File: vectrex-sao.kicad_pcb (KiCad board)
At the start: 2 copper layers, 78 parts, among them J2 Badgelife_sao_connector_v169b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, U1 PIC16F886-IP, U2 IS31FL3731-SALS2

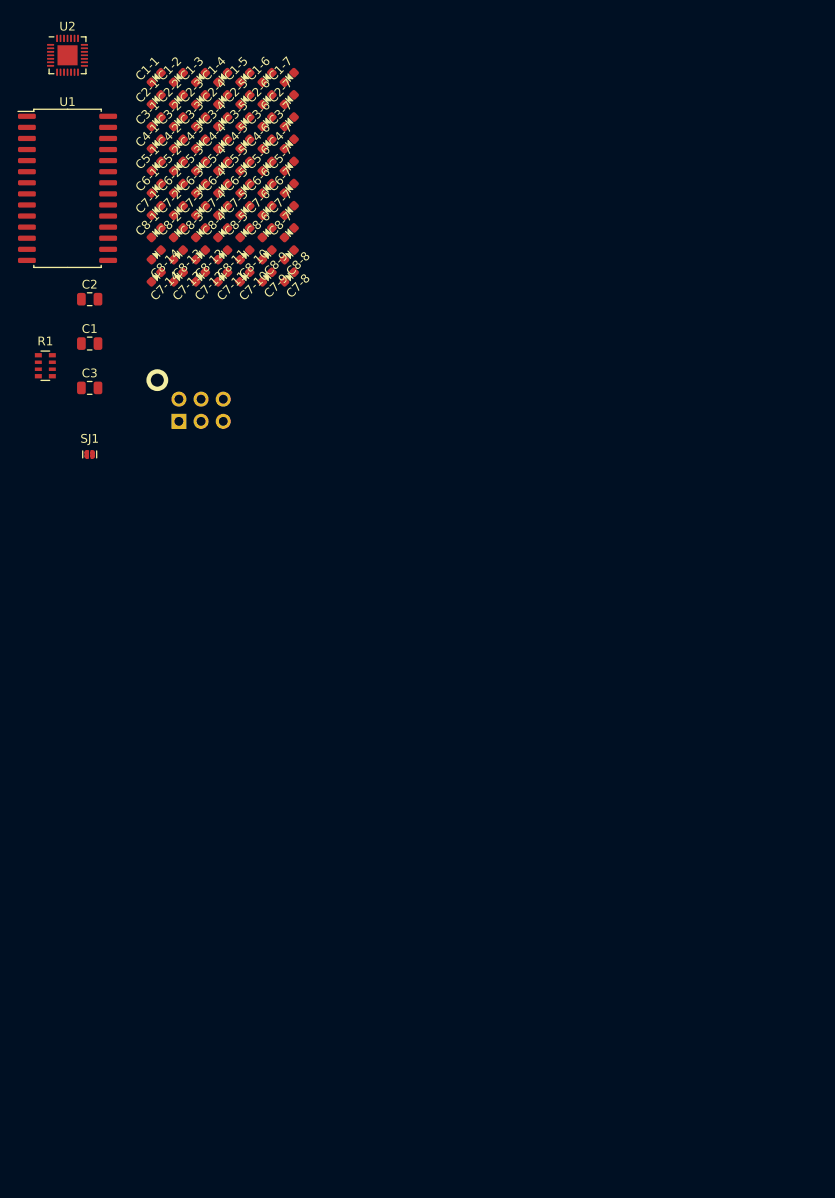
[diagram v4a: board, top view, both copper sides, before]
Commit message: rearranged parts, add temp silk, grid 2.54mm
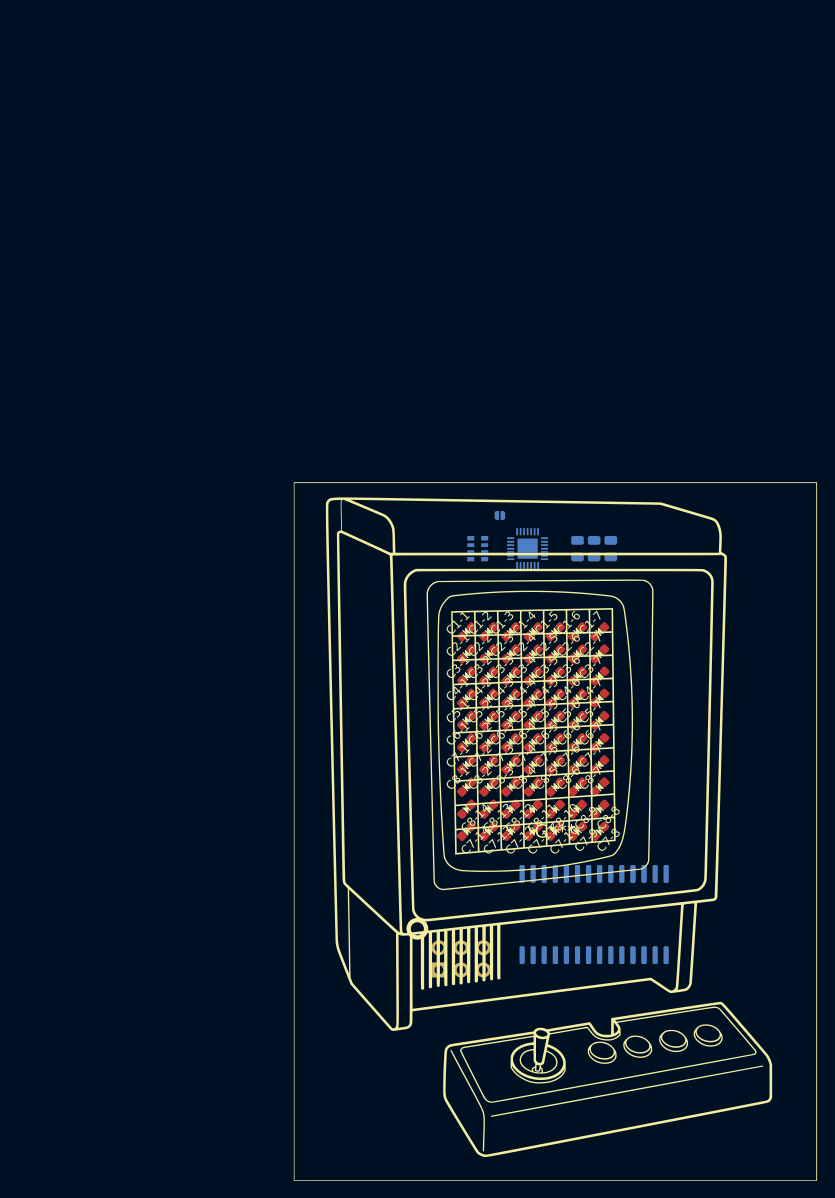
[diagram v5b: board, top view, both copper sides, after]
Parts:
- added G***: LOGO, LOGO, F.Cu at (127.0, 106.7)
- C1, C2, C3, R1, SJ1, U1, U2: moved to B.Cu
- moved U1 102.8 mm to (131.4, 116.2), turned to -90 degrees
- moved U2 77.3 mm to (123.8, 74.3), turned to 180 degrees
- moved C3-7 72.8 mm to (132.1, 88.9)
- moved C7-8 72.8 mm to (132.1, 106.7)
- moved C2-1 72.8 mm to (116.8, 86.4)
- moved C2-2 72.8 mm to (119.4, 86.4)
- moved C2-3 72.8 mm to (121.9, 86.4)
- moved C2-5 72.8 mm to (127.0, 86.4)
- moved C2-7 72.8 mm to (132.1, 86.4)
- moved C3-1 72.8 mm to (116.8, 88.9)
- moved C3-2 72.8 mm to (119.4, 88.9)
- moved C3-3 72.8 mm to (121.9, 88.9)
- moved C3-4 72.8 mm to (124.5, 88.9)
- moved C3-5 72.8 mm to (127.0, 88.9)
- moved C3-6 72.8 mm to (129.5, 88.9)
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
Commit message: finished outline, added controller board
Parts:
- removed the G*** at (127.0, 106.7)
- removed SJ1: SOLDERJUMPER, vectrex-sao:SolderJumper-2_P1.3mm_Open_RoundedPad1.0x1.5mm
- added C4: 0.1uF, Capacitor_SMD:C_0805_2012Metric, B.Cu at (115.0, 71.6)
- added C5: 0.1uF, Capacitor_SMD:C_0603_1608Metric, B.Cu at (124.0, 121.5)
- added C6: 22pF, Capacitor_SMD:C_0603_1608Metric, B.Cu at (126.2, 121.5)
- added G***: vectrex-graphic-console-80mm, vectrex-sao:vectrex-graphic-console-80mm, F.Cu at (125.9, 105.5)
- added J1: ICSP, Connector_PinHeader_2.54mm:PinHeader_1x06_P2.54mm_Vertical_SMD_Pin1Right, B.Cu at (106.1, 98.5)
- added JP1: TOUCH_PAD, vectrex-sao:MountingHole_1.5mm_M2_Pad_TopOnly, B.Cu at (133.8, 117.9)
- added JP3: ADDR, vectrex-sao:SolderJumper-2_P1.3mm_Open_RoundedPad1.0x1.5mm, B.Cu at (118.5, 71.0)
- added JP4: TX, vectrex-sao:SolderJumper-2_P1.3mm_Open_RoundedPad1.0x1.5mm, B.Cu at (106.0, 114.5)
- added JP5: RX, vectrex-sao:SolderJumper-2_P1.3mm_Open_RoundedPad1.0x1.5mm, B.Cu at (104.2, 114.5)
- added R2: 10k, Resistor_SMD:R_0603_1608Metric, B.Cu at (125.5, 115.5)
- added R3: 1k, Resistor_SMD:R_0603_1608Metric, B.Cu at (128.7, 120.8)
- added U3: TC233A, Package_TO_SOT_SMD:SOT-23-6, B.Cu at (125.1, 118.2)
- C1-1, C1-2, C1-3, C1-4, C1-5, C1-6, C1-7, C2-1, C2-2, C2-3, C2-4, C2-5, C2-6, C2-7, C3-1, C3-2, C3-3, C3-4, C3-5, C3-6, C3-7, C4-1, C4-2, C4-3, C4-4, C4-5, C4-6, C4-7, C5-1, C5-2, C5-3, C5-4, C5-5, C5-6, C5-7, C6-1, C6-2, C6-3, C6-4, C6-5, C6-6, C6-7, C7-1, C7-10, C7-11, C7-12, C7-13, C7-14, C7-2, C7-3, C7-4, C7-5, C7-6, C7-7, C7-8, C7-9, C8-1, C8-10, C8-11, C8-12, C8-13, C8-14, C8-2, C8-3, C8-4, C8-5, C8-6, C8-7, C8-8, C8-9: footprint vectrex-sao:C_0603_1608Metric -> vectrex-sao:LED_0603_1608Metric
- moved U1 44.3 mm to (107.8, 78.8), turned to 180 degrees
- moved J2 4.00 mm to (112.2, 120.7)
- moved C3 2.49 mm to (132.9, 71.8)
- moved C1 2.49 mm to (131.0, 71.9)
- moved C2 2.49 mm to (129.1, 71.9)
- moved U2 1.75 mm to (124.3, 72.6)
- moved C1-7 1.26 mm to (132.2, 82.6)
- moved C1-6 1.20 mm to (129.6, 82.6)
- moved C1-5 1.14 mm to (127.0, 82.7)
- moved C2-7 1.13 mm to (132.3, 85.2)
- moved C7-14 1.10 mm to (116.9, 107.8)
- moved C1-4 1.07 mm to (124.4, 82.8)
- moved C2-6 1.04 mm to (129.7, 85.3)
- moved C1-3 1.03 mm to (121.8, 82.8)
- moved C3-7 1.02 mm to (132.3, 87.9)
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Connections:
- J2 pad 3: /SDA -> unconnected-(J2-Pad3)
- J2 pad 4: /SCL -> unconnected-(J2-Pad4)
- J2 pad 5: /MISO -> /RX
- J2 pad 6: /SCLK -> /TX
- U1 pad 1: /n_MCLR -> /MCLR
- U1 pad 17: unconnected-(U1-Pad17) -> Net-(JP4-Pad2)
- U1 pad 18: unconnected-(U1-Pad18) -> Net-(JP5-Pad2)
- U1 pad 21: unconnected-(U1-Pad21) -> /TOUCH_UC
- U2 pad 29: (no net) -> GND
- U2 pad 5: GND -> unconnected-(U2-Pad5)
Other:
- board outline added: 46.8 x 62 mm

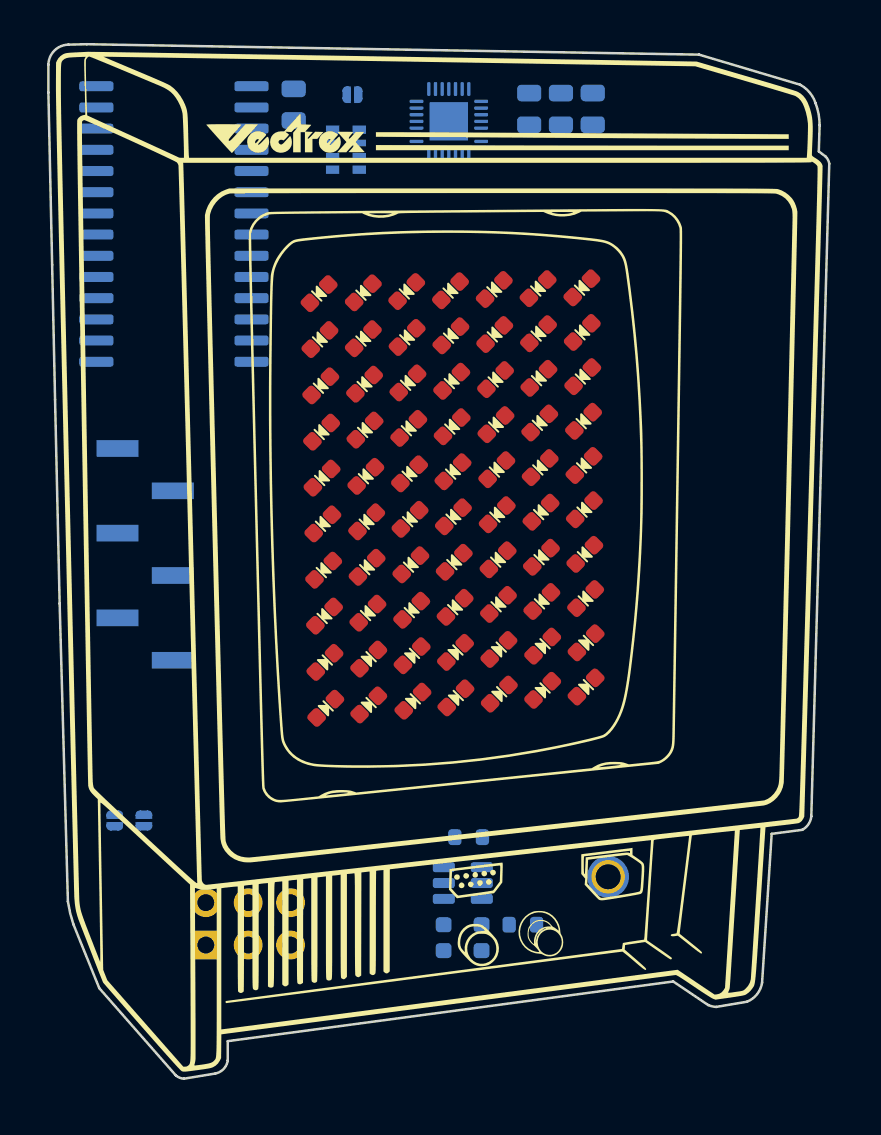
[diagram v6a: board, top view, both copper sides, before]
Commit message: updated models and created files for ordering
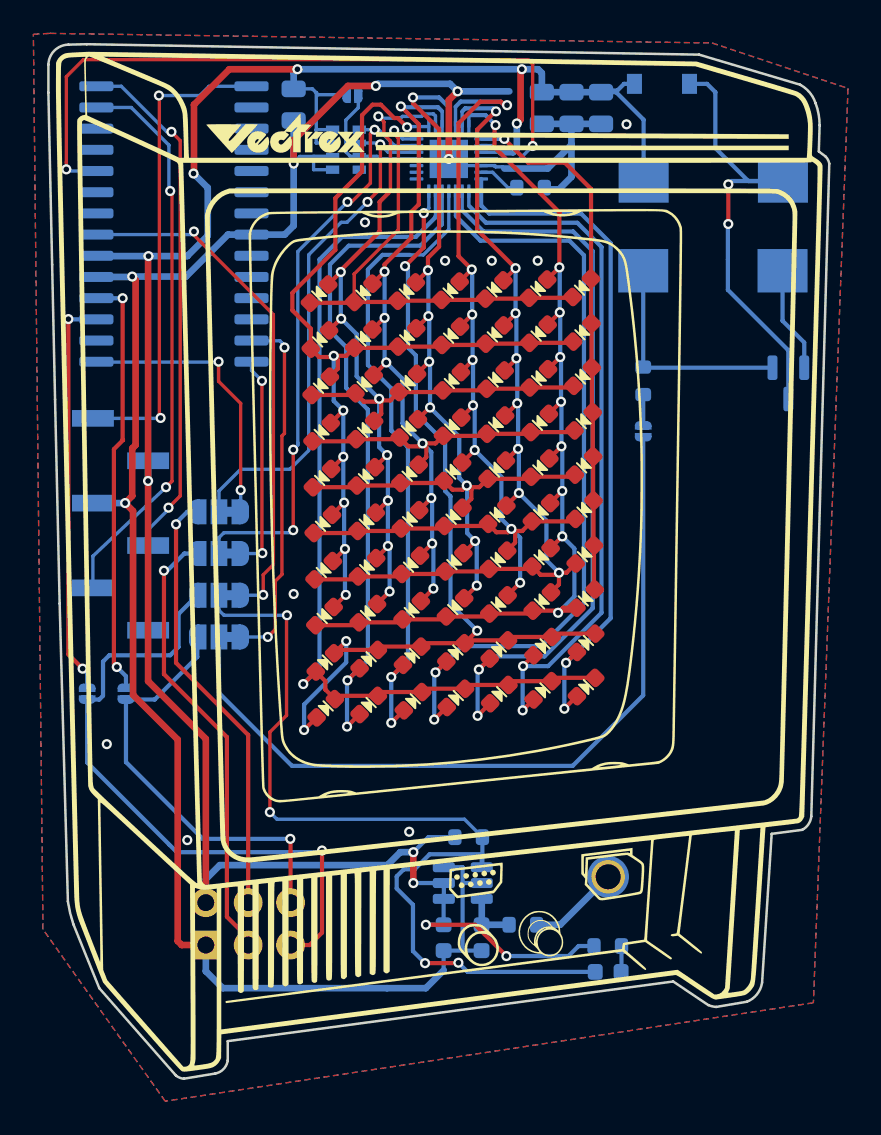
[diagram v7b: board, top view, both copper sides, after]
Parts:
- added D1: MBR0520, Diode_SMD:D_SOD-123, B.Cu at (137.1, 70.3)
- added G***: music-notes, vectrex-sao:music-notes, B.Cu at (140.2, 90.6)
- added G***: LOGO, LOGO, B.Cu at (124.6, 94.7)
- added JP2: solderjumper-3way, vectrex-sao:SolderJumper-3_P1.3mm_Bridged12_RoundedPad1.0x1.5mm_NumberLabels, B.Cu at (110.5, 96.0)
- added JP6: solderjumper-3way, vectrex-sao:SolderJumper-3_P1.3mm_Bridged12_RoundedPad1.0x1.5mm_NumberLabels, B.Cu at (110.5, 98.5)
- added JP7: solderjumper-3way, vectrex-sao:SolderJumper-3_P1.3mm_Bridged12_RoundedPad1.0x1.5mm_NumberLabels, B.Cu at (110.5, 101.0)
- added JP8: solderjumper-3way, vectrex-sao:SolderJumper-3_P1.3mm_Bridged12_RoundedPad1.0x1.5mm_NumberLabels, B.Cu at (110.5, 103.5)
- added JP9: SOUND, vectrex-sao:SolderJumper-2_P1.3mm_Open_RoundedPad1.0x1.5mm, B.Cu at (135.9, 91.2)
- added LED1: LED0603_NOOUTLINE, vectrex-sao:LED_0603_1608Metric, B.Cu at (133.8, 123.6)
- added LS1: Speaker FUET-9032-05, vectrex-sao:MagneticBuzzer_FUET-9032-05, B.Cu at (140.1, 78.2)
- added LS2: Speaker FUET-9032-05, vectrex-sao:MagneticBuzzer_FUET-9032-05, B.Cu at (140.1, 83.6)
- added Q1: MMBT3904, Package_TO_SOT_SMD:SOT-23, B.Cu at (144.6, 88.3)
- added R4: 1k, Resistor_SMD:R_0603_1608Metric, B.Cu at (133.8, 122.0)
- added R5: 1k, Resistor_SMD:R_0603_1608Metric, B.Cu at (135.9, 88.2)
- added R6: 10k, Resistor_SMD:R_0603_1608Metric, B.Cu at (129.2, 76.6)
- J2: value Badgelife_sao_connector_v169bis -> SAO_v169bis
- JP3: value ADDR -> 0x77
- moved JP4 8.33 mm to (102.6, 106.9)
- moved JP5 7.63 mm to (104.9, 106.9)
- moved J1 2.33 mm to (104.6, 96.8)
- moved U2 2.25 mm to (124.3, 74.8)
- moved C2 0.76 mm to (129.8, 71.8)
- moved C1 0.63 mm to (131.6, 71.8)
- moved C3 0.50 mm to (133.4, 71.8)
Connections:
- net /RX renamed /PWM_BADGE
- net /TX renamed /TOUCH_BADGE
- J2 pad 3: unconnected-(J2-Pad3) -> /SDA_BADGE
- J2 pad 4: unconnected-(J2-Pad4) -> /SCL_BADGE
- R1 pad 1: /SCL -> /SCL_LED
- R1 pad 2: /SDA -> /SDA_LED
- R1 pad 4: Net-(R1-Pad4) -> (no net)
- R1 pad 5: GND -> (no net)
- R2 pad 1: /TOUCH_UC -> /TOUCH_OUT
- U1 pad 13: unconnected-(U1-Pad13) -> /PWM_UC
- U1 pad 14: /SCL -> /SCL_UC
- U1 pad 15: /SDA -> /SDA_UC
- U1 pad 24: unconnected-(U1-Pad24) -> /LED_INT_UC
- U2 pad 19: /SDA -> /SDA_LED
- U2 pad 20: /SCL -> /SCL_LED
- U2 pad 4: /INTB -> /LED_INT_UC
- U2 pad 5: unconnected-(U2-Pad5) -> GND
- U2 pad 6: Net-(R1-Pad4) -> Net-(U2-Pad6)
- U3 pad 1: /TOUCH_UC -> /TOUCH_OUT
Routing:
- net +3.3V: track 0.00 -> 146.2 mm, vias 0 -> 10
- net GND: track 0.00 -> 143.7 mm, vias 0 -> 15
- net /CA6: track 0.00 -> 61.4 mm, vias 0 -> 8
- net /CA3: track 0.00 -> 59.9 mm, vias 0 -> 8
- net /CA5: track 0.00 -> 59.5 mm, vias 0 -> 8
- net /CA4: track 0.00 -> 59.4 mm, vias 0 -> 8
- net /CA2: track 0.00 -> 59.0 mm, vias 0 -> 7
- net /CA8: track 0.00 -> 58.6 mm, vias 0 -> 9
- net /CA7: track 0.00 -> 57.3 mm, vias 0 -> 8
- net /TOUCH_OUT: track 0.00 -> 55.3 mm, vias 0 -> 4
- net /CB7: track 0.00 -> 54.8 mm, vias 0 -> 1
- net /CB8: track 0.00 -> 54.4 mm, vias 0 -> 5
- net /PWM_IN: track 0.00 -> 47.8 mm
- net /CB4: track 0.00 -> 46.5 mm, vias 0 -> 2
- net /CB3: track 0.00 -> 44.5 mm, vias 0 -> 2
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- added copper zone on B.Cu, net GND
- added copper zone on F.Cu, net GND
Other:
- board text added: "3V3"
- board text added: "BADGE"
- board text added: "CLK"
- board text added: "DAT"
- board text added: "GND"
- board text added: "JLCJLCJLCJLCJLC"
- board text added: "Jay Smith - Vectrex Creator"
- board text added: "MCLR"
- board text added: "NC"
- board text added: "SAO"
- board text added: "SDA SCL TOUCH PWM"
- board text added: "SOUND"
- board text added: "Vectrex SAO - Supercon '22"
- board text added: "github.com/technobly/vectrex-sao"
